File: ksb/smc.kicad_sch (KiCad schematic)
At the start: 16 parts, among them J13 Conn_01x04, U4 X850744-001

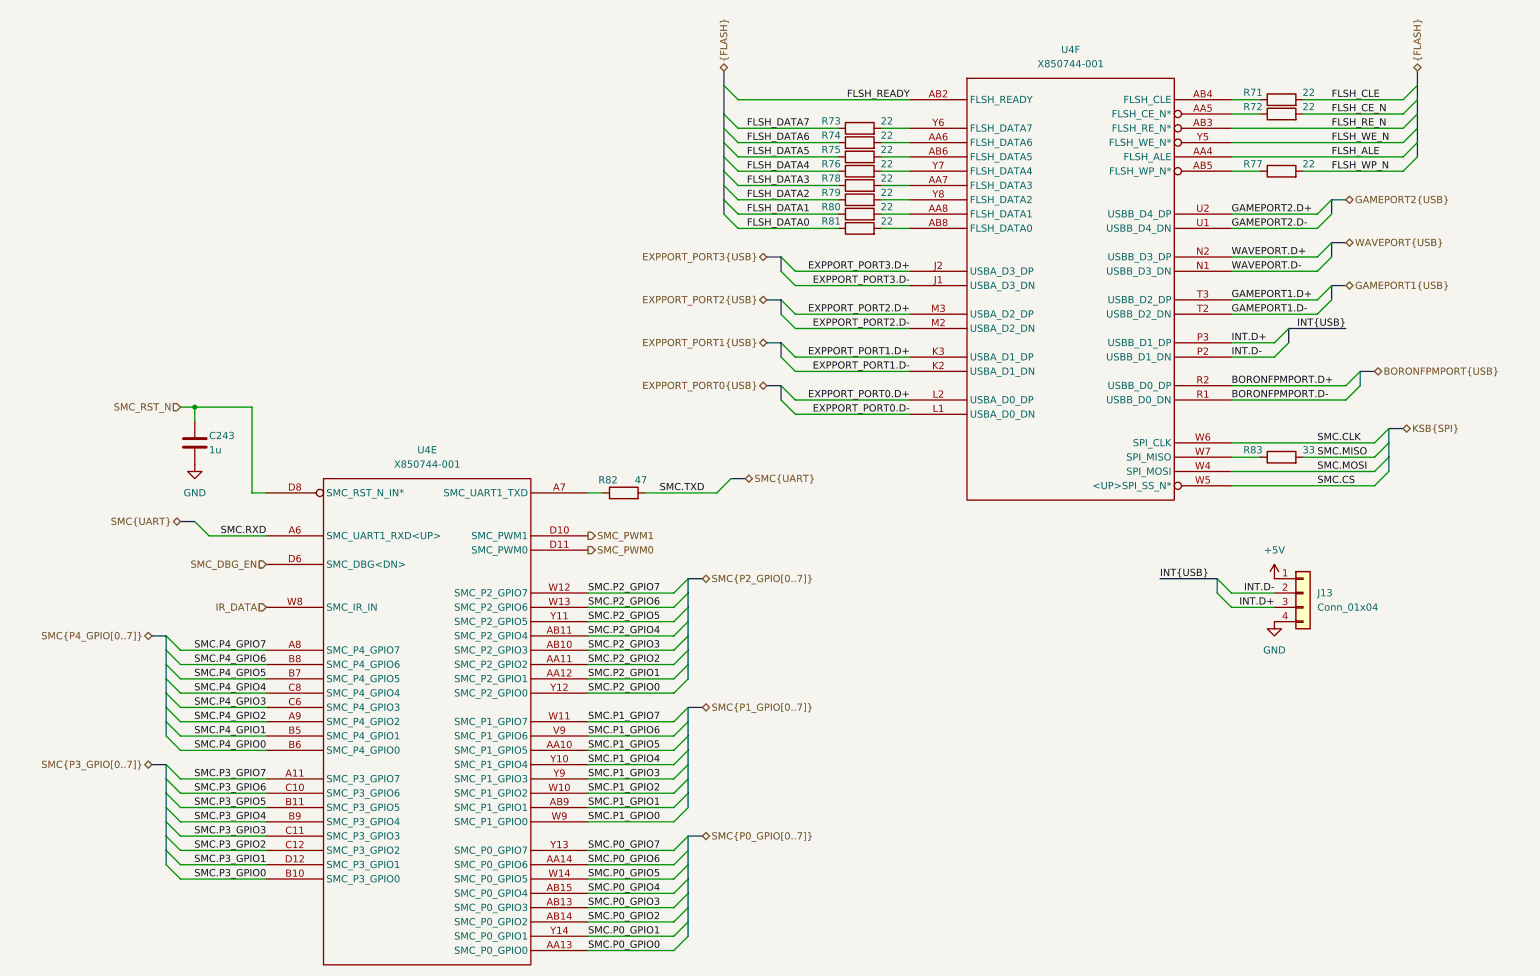
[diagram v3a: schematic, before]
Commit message: Multipurpose and standby power rails, Reannotated schematic
Added V_1P2, V_1P8, V_5P0DUAL, V_EFUSE, V_GPUPCIE, V_3P3STBY and V_1P2STBY
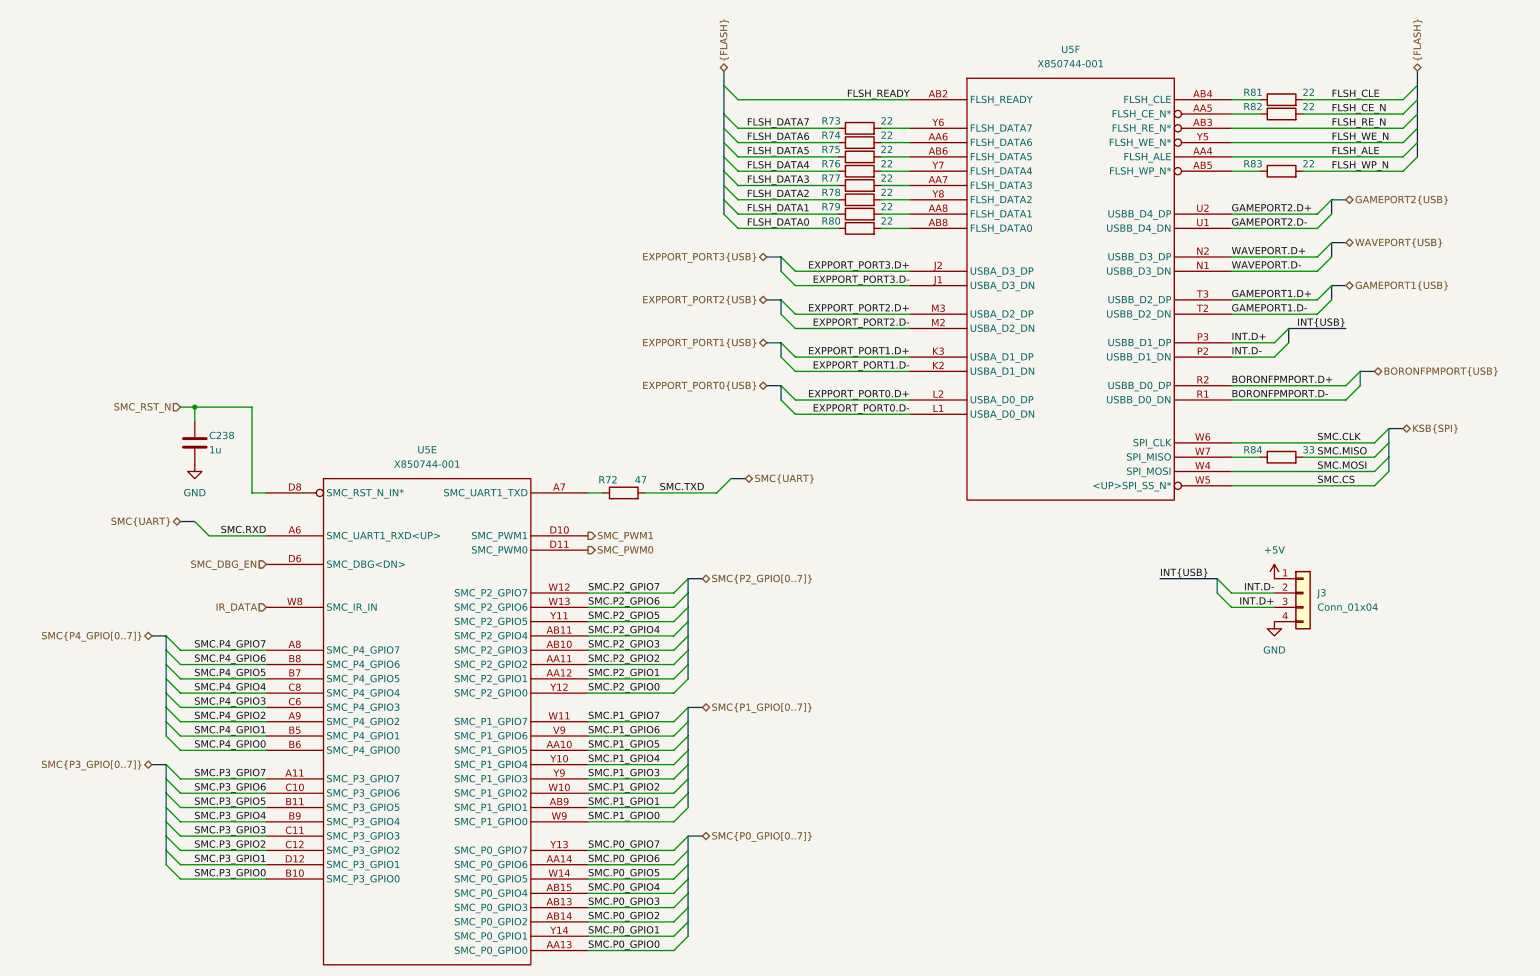
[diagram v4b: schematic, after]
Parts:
- renumbered C243 to C238, J13 to J3, R82 to R72, R78 to R77, R79 to R78, R80 to R79, R81 to R80, R71 to R81, R72 to R82, R77 to R83, R83 to R84, U4 to U5
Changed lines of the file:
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@@
 		(on_board yes)
 		(dnp no)
-		(property "Reference" "C243"
+		(property "Reference" "C238"
 			(at 50.8 92.71 0)
 			(effects
@@
 			(project "StingBurst"
 				(path "/16640ecb-e4a4-4594-871b-70047bfba6e0/5578fb0d-7a85-48a3-97bd-11e67ac7c8dc/c36da264-812f-4670-a9cc-d1fe224eb93b"
-					(reference "C243")
+					(reference "C238")
 					(unit 1)
 				)
@@
 		(dnp no)
 		(fields_autoplaced yes)
-		(property "Reference" "#PWR0398"
+		(property "Reference" "#PWR0114"
 			(at 240.03 121.92 0)
 			(effects
@@
 			(project ""
 				(path "/16640ecb-e4a4-4594-871b-70047bfba6e0/5578fb0d-7a85-48a3-97bd-11e67ac7c8dc/c36da264-812f-4670-a9cc-d1fe224eb93b"
-					(reference "#PWR0398")
+					(reference "#PWR0114")
 					(unit 1)
 				)
@@
 		(on_board yes)
 		(dnp no)
-		(property "Reference" "R81"
+		(property "Reference" "R80"
 			(at 161.29 54.61 90)
 			(effects
@@
 			(project "StingBurst"
 				(path "/16640ecb-e4a4-4594-871b-70047bfba6e0/5578fb0d-7a85-48a3-97bd-11e67ac7c8dc/c36da264-812f-4670-a9cc-d1fe224eb93b"
-					(reference "R81")
+					(reference "R80")
 					(unit 1)
 				)
@@
 		(dnp no)
 		(fields_autoplaced yes)
-		(property "Reference" "#PWR0111"
+		(property "Reference" "#PWR0113"
 			(at 48.26 104.14 0)
 			(effects
@@
 			(project ""
 				(path "/16640ecb-e4a4-4594-871b-70047bfba6e0/5578fb0d-7a85-48a3-97bd-11e67ac7c8dc/c36da264-812f-4670-a9cc-d1fe224eb93b"
-					(reference "#PWR0111")
+					(reference "#PWR0113")
 					(unit 1)
 				)
@@
 		(on_board yes)
 		(dnp no)
-		(property "Reference" "R77"
+		(property "Reference" "R83"
 			(at 236.22 44.45 90)
 			(effects
@@
 			(project "StingBurst"
 				(path "/16640ecb-e4a4-4594-871b-70047bfba6e0/5578fb0d-7a85-48a3-97bd-11e67ac7c8dc/c36da264-812f-4670-a9cc-d1fe224eb93b"
-					(reference "R77")
+					(reference "R83")
 					(unit 1)
 				)
@@
 		(on_board yes)
 		(dnp no)
-		(property "Reference" "R80"
+		(property "Reference" "R79"
 			(at 161.29 52.07 90)
 			(effects
@@
 			(project "StingBurst"
 				(path "/16640ecb-e4a4-4594-871b-70047bfba6e0/5578fb0d-7a85-48a3-97bd-11e67ac7c8dc/c36da264-812f-4670-a9cc-d1fe224eb93b"
-					(reference "R80")
+					(reference "R79")
 					(unit 1)
 				)
@@
 		(on_board yes)
 		(dnp no)
-		(property "Reference" "R78"
+		(property "Reference" "R77"
 			(at 161.29 46.99 90)
 			(effects
@@
 			(project "StingBurst"
 				(path "/16640ecb-e4a4-4594-871b-70047bfba6e0/5578fb0d-7a85-48a3-97bd-11e67ac7c8dc/c36da264-812f-4670-a9cc-d1fe224eb93b"
-					(reference "R78")
+					(reference "R77")
 					(unit 1)
 				)
@@
 		(on_board yes)
 		(dnp no)
-		(property "Reference" "R79"
+		(property "Reference" "R78"
 			(at 161.29 49.53 90)
 			(effects
@@
 			(project "StingBurst"
 				(path "/16640ecb-e4a4-4594-871b-70047bfba6e0/5578fb0d-7a85-48a3-97bd-11e67ac7c8dc/c36da264-812f-4670-a9cc-d1fe224eb93b"
-					(reference "R79")
+					(reference "R78")
 					(unit 1)
 				)
@@
 		(dnp no)
 		(fields_autoplaced yes)
-		(property "Reference" "J13"
+		(property "Reference" "J3"
 			(at 247.65 120.6499 0)
 			(effects
@@
 			(project ""
 				(path "/16640ecb-e4a4-4594-871b-70047bfba6e0/5578fb0d-7a85-48a3-97bd-11e67ac7c8dc/c36da264-812f-4670-a9cc-d1fe224eb93b"
-					(reference "J13")
+					(reference "J3")
 					(unit 1)
 				)
@@
 		(on_board yes)
 		(dnp no)
-		(property "Reference" "U4"
+		(property "Reference" "U5"
 			(at 89.535 95.25 0)
 			(effects
@@
 			(project ""
 				(path "/16640ecb-e4a4-4594-871b-70047bfba6e0/5578fb0d-7a85-48a3-97bd-11e67ac7c8dc/c36da264-812f-4670-a9cc-d1fe224eb93b"
-					(reference "U4")
+					(reference "U5")
 					(unit 5)
 				)
@@
 		(dnp no)
 		(fields_autoplaced yes)
-		(property "Reference" "U4"
+		(property "Reference" "U5"
 			(at 203.835 24.13 0)
 			(effects
@@
 			(project ""
 				(path "/16640ecb-e4a4-4594-871b-70047bfba6e0/5578fb0d-7a85-48a3-97bd-11e67ac7c8dc/c36da264-812f-4670-a9cc-d1fe224eb93b"
-					(reference "U4")
+					(reference "U5")
 					(unit 6)
 				)
@@
 		(on_board yes)
 		(dnp no)
-		(property "Reference" "R71"
+		(property "Reference" "R81"
 			(at 236.22 31.75 90)
 			(effects
@@
 			(project "StingBurst"
 				(path "/16640ecb-e4a4-4594-871b-70047bfba6e0/5578fb0d-7a85-48a3-97bd-11e67ac7c8dc/c36da264-812f-4670-a9cc-d1fe224eb93b"
-					(reference "R71")
+					(reference "R81")
 					(unit 1)
 				)
@@
 		(on_board yes)
 		(dnp no)
-		(property "Reference" "R83"
+		(property "Reference" "R84"
 			(at 236.22 95.25 90)
 			(effects
@@
 			(project "StingBurst"
 				(path "/16640ecb-e4a4-4594-871b-70047bfba6e0/5578fb0d-7a85-48a3-97bd-11e67ac7c8dc/c36da264-812f-4670-a9cc-d1fe224eb93b"
-					(reference "R83")
+					(reference "R84")
 					(unit 1)
 				)
@@
 		(dnp no)
 		(fields_autoplaced yes)
-		(property "Reference" "#PWR0399"
+		(property "Reference" "#PWR0115"
 			(at 240.03 132.08 0)
 			(effects
@@
 			(project ""
 				(path "/16640ecb-e4a4-4594-871b-70047bfba6e0/5578fb0d-7a85-48a3-97bd-11e67ac7c8dc/c36da264-812f-4670-a9cc-d1fe224eb93b"
-					(reference "#PWR0399")
+					(reference "#PWR0115")
 					(unit 1)
 				)
@@
 		(on_board yes)
 		(dnp no)
-		(property "Reference" "R82"
+		(property "Reference" "R72"
 			(at 121.666 100.584 90)
 			(effects
@@
 			(project "StingBurst"
 				(path "/16640ecb-e4a4-4594-871b-70047bfba6e0/5578fb0d-7a85-48a3-97bd-11e67ac7c8dc/c36da264-812f-4670-a9cc-d1fe224eb93b"
-					(reference "R82")
+					(reference "R72")
 					(unit 1)
 				)
@@
 		(on_board yes)
 		(dnp no)
-		(property "Reference" "R72"
+		(property "Reference" "R82"
 			(at 236.22 34.29 90)
 			(effects
@@
 			(project "StingBurst"
 				(path "/16640ecb-e4a4-4594-871b-70047bfba6e0/5578fb0d-7a85-48a3-97bd-11e67ac7c8dc/c36da264-812f-4670-a9cc-d1fe224eb93b"
-					(reference "R72")
+					(reference "R82")
 					(unit 1)
 				)
